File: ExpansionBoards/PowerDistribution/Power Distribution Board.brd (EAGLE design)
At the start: 160 x 74.6 mm, 27 parts, among them J1 350211-1, J10 640445-3, J11 640445-5, J12 640445-8, J13 640445-6, J2 216571-2005, J3 216571-2004, J4 216571-2003, J5 350211-1, J6 216571-2002, J7 216571-2008, J8 640445-4, J9 640445-2, K1 AHQSS105DM2FA0G, U3 LM338T/NOPB

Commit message: expansion board improvements
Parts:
- added J14: 216571-2003, SamacSys_Parts:216571-YY03_1
- J8: value 640445-4 -> 640445-6; device SamacSys_Parts:SHDR4W117P0X396_1X4_1585X762X1 -> SamacSys_Parts:SHDR6W183P0X396_1X6_2377X762X1
- moved K1 17.8 mm to (17.8, 21.3), turned to 0 degrees
- moved J8 4.83 mm to (5.59, 40.4), turned to 90 degrees
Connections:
- net 12V: now also J8.5; no longer J8.4
- net 5V: now also J8.6; no longer J8.1
- net GND: now also J14.2, J8.1, J8.4
- net LINE_HOT_IN: now also J14.3
- net LINE_NEUTRAL: now also J14.1
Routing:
- net LINE_NEUTRAL: track 92.9 -> 115.7 mm
- net LINE_HOT_IN: track 0.00 -> 20.4 mm
- net 12VPC: track 28.0 -> 13.6 mm
- net LINE_HOT: track 133.7 -> 125.2 mm
- net 5V: track 153.3 -> 159.6 mm
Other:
- board text added: "120VAC LINE IN"
- board text added: "PINSCAPE POWER DISTRIBUTION BOARD"
- board text added: "REV 20250106"

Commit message: add logo image
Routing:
- net GND: track 0.00 -> 83.5 mm

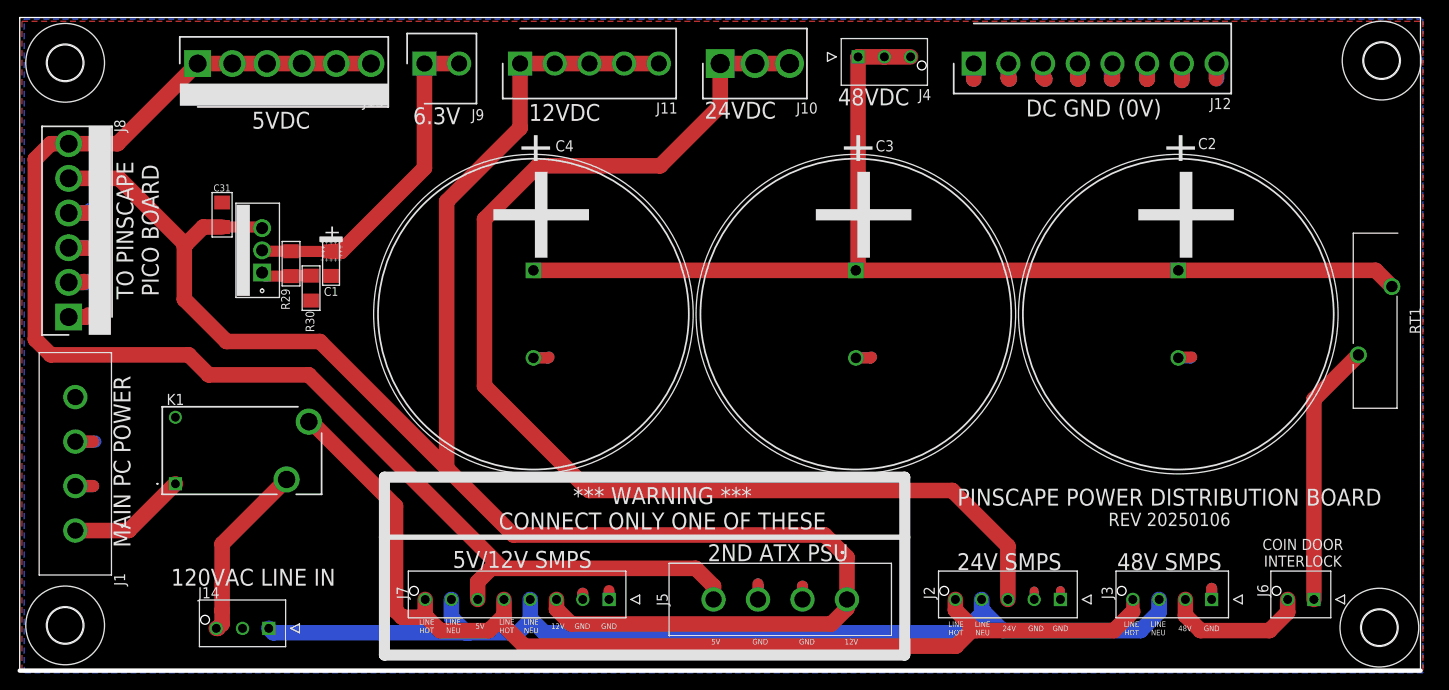
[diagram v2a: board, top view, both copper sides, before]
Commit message: Add ButtonLatencyTester2
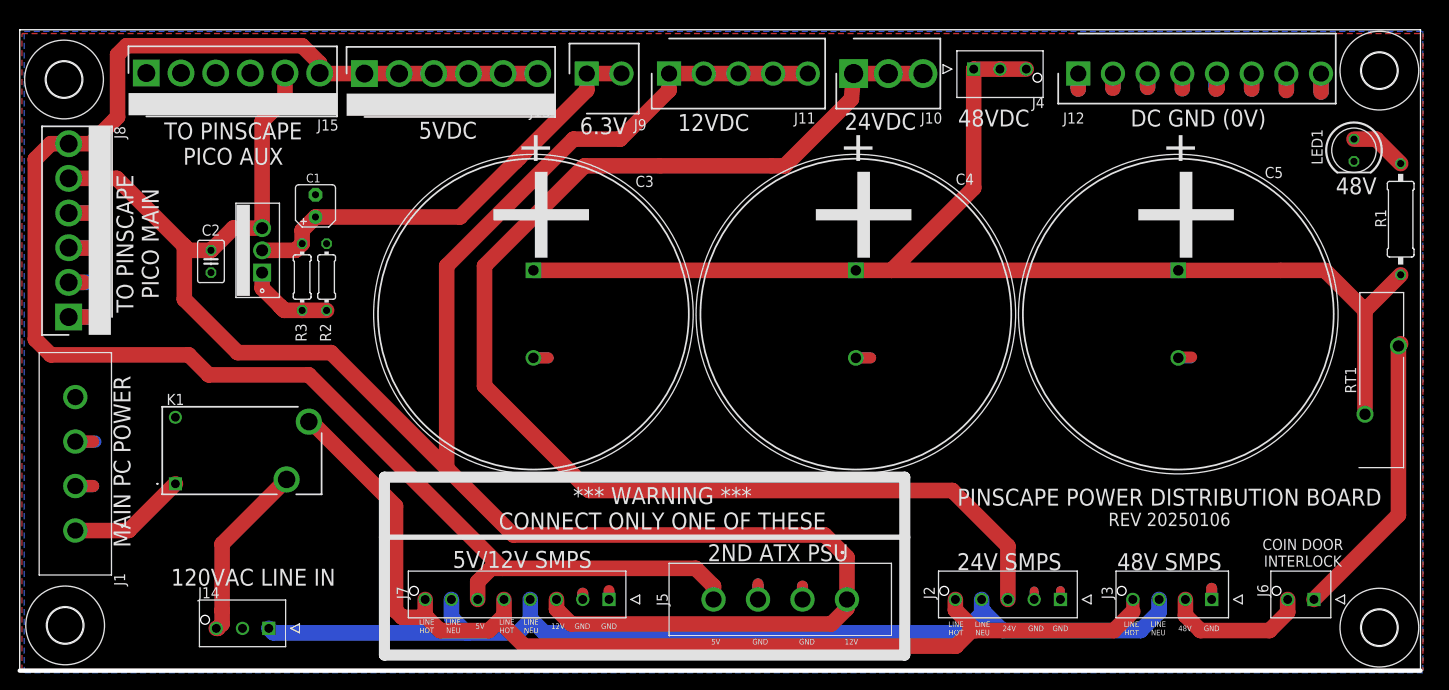
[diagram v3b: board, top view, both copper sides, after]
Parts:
- removed C31: 0.1uF, rcl:C1206
- removed R29: 270R, rcl:R1206
- removed R30: 1.1K, rcl:R1206
- added C5: SLPX682M080H7P3, SamacSys_Parts:CAPPRD1000W100D3550H4200
- added J15: 640445-6, SamacSys_Parts:SHDR6W183P0X396_1X6_2377X762X1
- added LED1: (no value), led:LED5MM
- added R1: 2.4K/1W, rcl:0309/12
- added R2: 1.1K, rcl:0204/7
- added R3: 270R, rcl:0204/7
- C1: device rcl:C1206_POL -> rcl:B45181A
- C2: value SLPX682M080H7P3 -> 0.1uF; device SamacSys_Parts:CAPPRD1000W100D3550H4200 -> rcl:C025-030X050
- moved C2 110.5 mm to (21.8, 46.7)
- moved C3 36.8 mm to (58.7, 45.7)
- moved C4 36.8 mm to (95.5, 45.7)
- moved J13 19.1 mm to (39.4, 68.2)
- moved J9 18.6 mm to (64.8, 68.2)
- moved J11 17.1 mm to (74.2, 68.2)
- moved J10 15.3 mm to (95.2, 68.2)
- moved J4 13.3 mm to (109.0, 68.7)
- moved J12 12.0 mm to (120.9, 68.2)
- moved C1 6.84 mm to (33.8, 53.1), turned to 90 degrees
- moved RT1 4.68 mm to (157.5, 37.1), turned to 270 degrees
- moved U$3 1.91 mm to (5.06, 67.5)
- moved U$1 1.17 mm to (155.3, 68.5)
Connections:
- new net N$3: LED1.A, R1.1
- net 12V: now also C2.1, J15.5; no longer C31.1
- net 48V: now also C5.1, R1.2; no longer C2.1
- net 5V: now also J15.6
- net 6V3: now also R3.2; no longer R29.2
- net GND: now also C5.2, J15.1, J15.2, J15.3, J15.4, LED1.K, R2.1; no longer C31.2, R30.1
- net N$32: now also R2.2, R3.1; no longer R29.1, R30.2
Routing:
- net 12V: track 227.7 -> 255.7 mm
- net 5V: track 159.6 -> 185.6 mm
- net 48V: track 129.4 -> 147.4 mm
- net 6V3: track 38.5 -> 51.4 mm
- net 24V: track 137.5 -> 147.8 mm
- net N$3: track 0.00 -> 6.49 mm
- net N$32: track 5.78 -> 10.2 mm
- net N$2: track 30.0 -> 33.3 mm
- net GND: track 83.5 -> 81.3 mm
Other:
- board size 160 x 74.6 mm -> 160 x 73.2 mm
- board text added: "TO PINSCAPE PICO AUX"
- board text added: "TO PINSCAPE PICO MAIN"
- board text removed: "TO PINSCAPE PICO BOARD"

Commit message: PCB parts lists (BOMs); power distro board edits
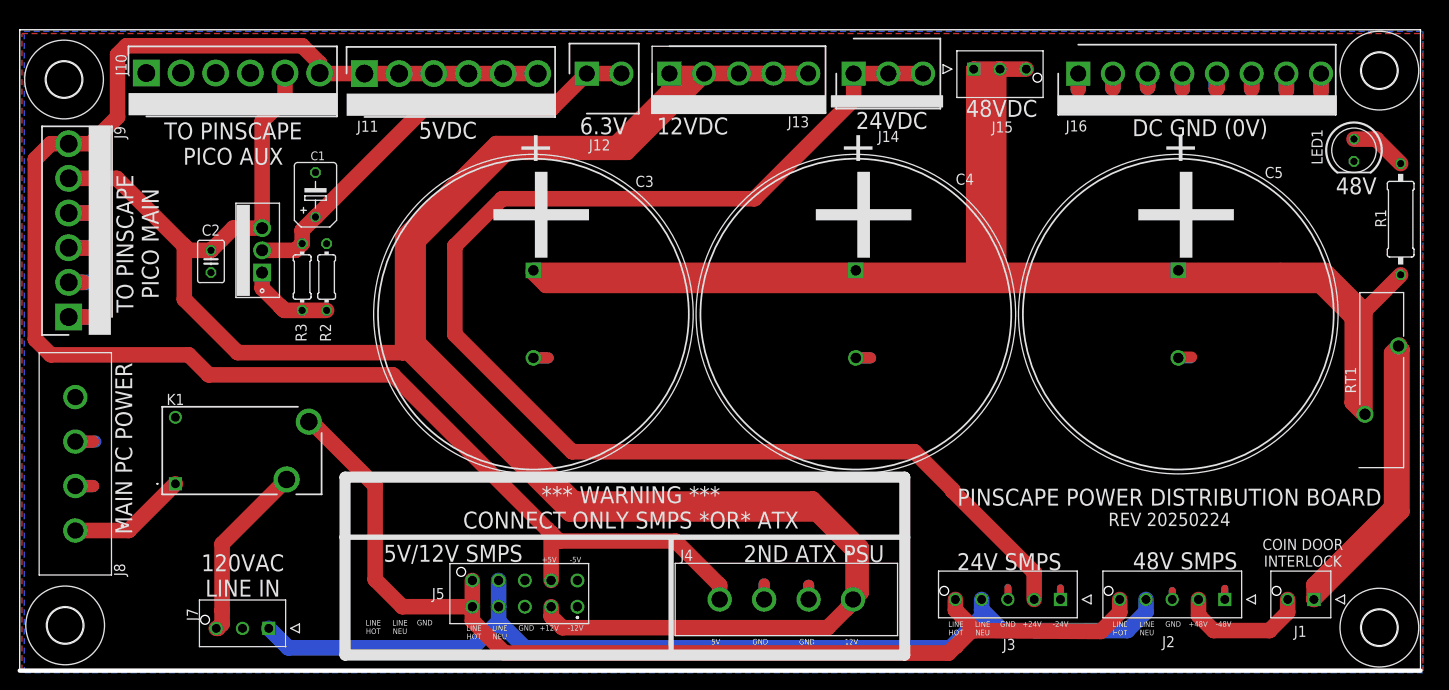
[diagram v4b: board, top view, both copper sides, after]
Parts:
- removed J6: 216571-2002, SamacSys_Parts:216571-YY02_1
- added J16: 640445-8, SamacSys_Parts:SHDR8W117P0X396_1X8_3170X762X1
- C1: device rcl:B45181A -> rcl:B45181B
- J1: value 350211-1 -> 216571-2002; device SamacSys_Parts:3502111 -> SamacSys_Parts:216571-YY02_1
- J10: value 640445-3 -> 640445-6; device SamacSys_Parts:HDRV3W140P0X396_1X3_1189X762X1 -> SamacSys_Parts:SHDR6W183P0X396_1X6_2377X762X1
- J11: value 640445-5 -> 640445-6; device SamacSys_Parts:HDRV5W117P0X396_1X5_1981X762X1 -> SamacSys_Parts:SHDR6W183P0X396_1X6_2377X762X1
- J12: value 640445-8 -> 640445-2; device SamacSys_Parts:SHDR8W117P0X396_1X8_3170X762X1 -> SamacSys_Parts:SHDR2W117P0X396_1X2_792X762X11
- J13: value 640445-6 -> 640445-5; device SamacSys_Parts:SHDR6W183P0X396_1X6_2377X762X1 -> SamacSys_Parts:HDRV5W117P0X396_1X5_1981X762X1
- J14: value 216571-2003 -> 640445-3; device SamacSys_Parts:216571-YY03_1 -> SamacSys_Parts:HDRV3W140P0X396_1X3_1189X762X1
- J15: value 640445-6 -> 216571-2003; device SamacSys_Parts:SHDR6W183P0X396_1X6_2377X762X1 -> SamacSys_Parts:216571-YY03_1
- J3: value 216571-2004 -> 216571-2005; device SamacSys_Parts:216571-YY04_1 -> SamacSys_Parts:216571-YY05_1
- J4: value 216571-2003 -> 350211-1; device SamacSys_Parts:216571-YY03_1 -> SamacSys_Parts:3502111
- J5: value 350211-1 -> 206832-1001; device SamacSys_Parts:3502111 -> SamacSys_Parts:2068321001
- J7: value 216571-2008 -> 216571-2003; device SamacSys_Parts:216571-YY08_1 -> SamacSys_Parts:216571-YY03_1
- J8: value 640445-6 -> 350211-1; device SamacSys_Parts:SHDR6W183P0X396_1X6_2377X762X1 -> SamacSys_Parts:3502111
- J9: value 640445-2 -> 640445-6; device SamacSys_Parts:SHDR2W117P0X396_1X2_792X762X11 -> SamacSys_Parts:SHDR6W183P0X396_1X6_2377X762X1
- moved J1 141.7 mm to (147.8, 8.13), turned to 0 degrees
- moved J15 94.5 mm to (109.0, 68.7), turned to 180 degrees
- moved J14 92.1 mm to (95.2, 68.2)
- moved J10 80.8 mm to (14.5, 68.3)
- moved J9 65.4 mm to (5.59, 40.4), turned to 90 degrees
- moved J4 62.1 mm to (95.2, 8.13), turned to 0 degrees
- moved J12 56.1 mm to (64.8, 68.2), turned to 0 degrees
- moved J13 42.8 mm to (82.1, 68.2), turned to 180 degrees
- moved J7 39.0 mm to (28.4, 4.83)
- moved J11 34.8 mm to (39.4, 68.2)
- moved J5 30.8 mm to (63.7, 7.30)
- moved J8 24.4 mm to (6.35, 16.0), turned to 270 degrees
- moved J2 18.8 mm to (137.6, 8.13)
- moved J3 17.3 mm to (118.9, 8.13)
- moved C1 1.27 mm to (33.8, 54.4)
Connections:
- net 12V: now also J10.5, J13.1, J13.2, J13.3, J13.4, J13.5, J4.1, J5.2, J9.5; no longer J11.1, J11.2, J11.3, J11.4, J11.5, J15.5, J5.1, J7.3, J8.5
- net 12VPC: now also J8.1; no longer J1.1
- net 24V: now also J14.1, J14.2, J14.3, J3.2; no longer J10.1, J10.2, J10.3, J2.3
- net 48V: now also J15.1, J15.2, J15.3; no longer J4.1, J4.2, J4.3
- net 5V: now also J10.6, J11.1, J11.2, J11.3, J11.4, J11.5, J11.6, J4.4, J5.7, J9.6; no longer J13.1, J13.2, J13.3, J13.4, J13.5, J13.6, J15.6, J5.4, J7.6, J8.6
- net 5VPC: now also J8.4; no longer J1.4
- net 6V3: now also J12.1, J12.2; no longer J9.1, J9.2
- net GND: now also J10.1, J10.2, J10.3, J10.4, J16.1, J16.2, J16.3, J16.4, J16.5, J16.6, J16.7, J16.8, J2.3, J3.3, J4.2, J4.3, J5.1, J5.6, J5.8, J9.1, J9.2, J9.3, J9.4; no longer J1.2, J1.3, J12.1, J12.2, J12.3, J12.4, J12.5, J12.6, J12.7, J12.8, J14.2, J15.1, J15.2, J15.3, J15.4, J2.2, J5.2, J7.1, J8.1, J8.4
- net LINE_HOT: now also J3.5, J5.10, J5.5; no longer J3.4, J7.5, J7.8
- net LINE_HOT_IN: now also J7.3; no longer J14.3
- net LINE_NEUTRAL: now also J3.4, J5.4, J5.9, J7.1; no longer J14.1, J3.3, J7.4, J7.7
- net N$1: now also J1.2, J2.2; no longer J3.2, J6.2
- net N$2: now also J1.1; no longer J6.1
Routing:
- net 48V: track 147.4 -> 297.9 mm
- net 12V: track 255.7 -> 374.4 mm
- net N$2: track 33.3 -> 66.4 mm
- net 24V: track 147.8 -> 154.1 mm
- net LINE_HOT: track 125.2 -> 121.6 mm
- net N$1: track 16.6 -> 15.1 mm
- net 6V3: track 51.4 -> 50.3 mm
- net 5V: track 185.6 -> 186.3 mm
- net LINE_NEUTRAL: track 115.7 -> 115.0 mm
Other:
- board text added: "*** WARNING *** CONNECT ONLY SMPS *OR* ATX"
- board text added: "+12V"
- board text added: "+24V"
- board text added: "+48V"
- board text added: "+5V"
- board text added: "-12V"
- board text added: "-24V"
- board text added: "-48V"
- board text added: "-5V"
- board text added: "REV 20250224"
- board text removed: "*** WARNING *** CONNECT ONLY ONE OF THESE"
- board text removed: "24V"
- board text removed: "REV 20250106"
